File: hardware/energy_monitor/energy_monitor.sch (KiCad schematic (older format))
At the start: 46 parts, among them J1 Screw_Terminal_01x03, U1 RAC04, U2 ADS131E08

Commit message: Working on schematic
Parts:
- added C10, C11, C12, C17, C18, C19, C20, C21, C22, C23, C24, C26, C27, C28, C29, C3, C4, C5, C6, C7, C8: C, symbol C
- added D1, D10, D11, D12, D13, D14, D15, D16, D2, D3, D4, D5, D6, D7, D8, D9: BAV99, symbol D_Schottky_x2_Serial_AKC
- added D? (x6): D_TVS, symbol D_TVS
- added J2, J3, J4, J5, J6, J7: Audio-Jack-3, symbol Audio-Jack-3
- added R10, R13, R14, R15, R16, R17, R18, R19, R20, R21, R22, R23, R24, R25, R26, R27, R28, R29, R30, R9: R, symbol R
- gave numbers to parts that had none: 35
- renumbered C1 to C13, C2 to C14, C3 to C15, C4 to C16, U2 to U4
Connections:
- net labels added: I1_N, I1_P, I2_N, I2_P, I3_N, I3_P, I4_N, I4_P, I5_N, I5_P, I6_N, I6_P, L2_N, L2_P
- wire segments 139 -> 341
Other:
- moved on the sheet: C1, C13, C14, C15, C16, C2, C25, C30, C31, C32, C33, C34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

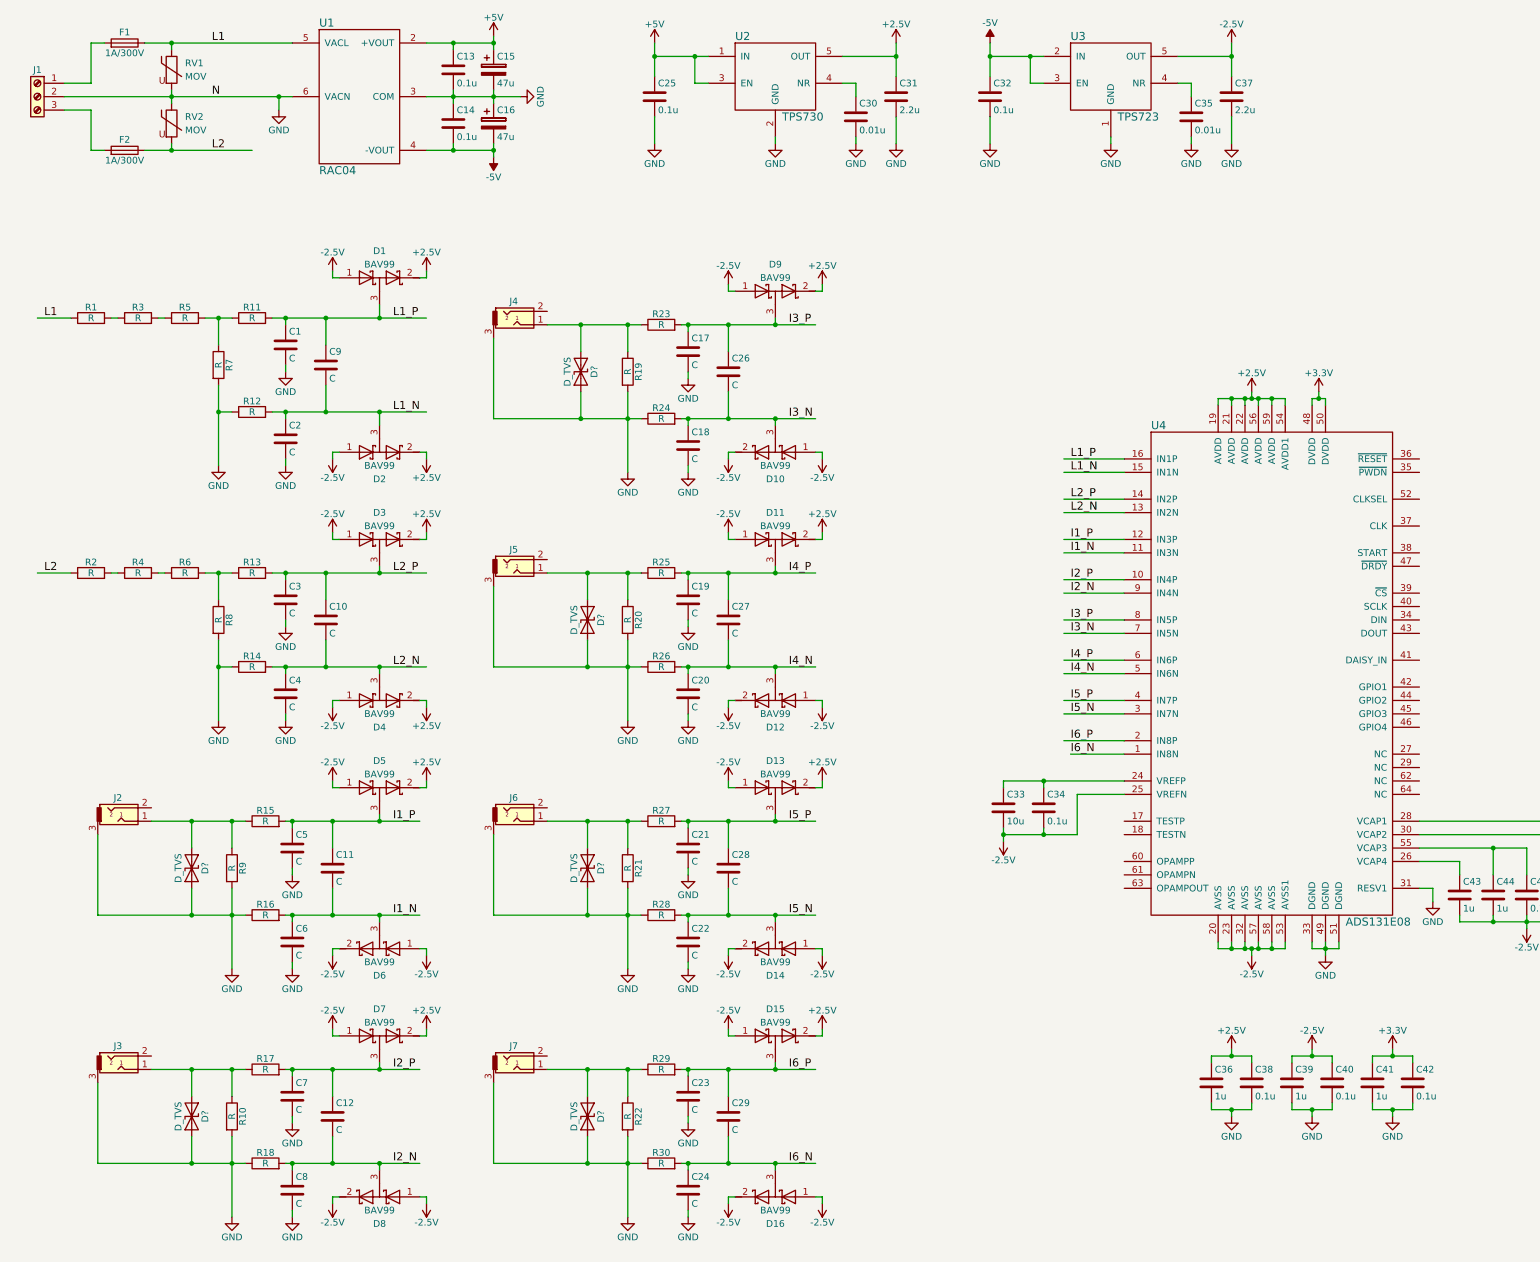
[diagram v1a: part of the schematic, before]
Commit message: Added footprints and part numbers for signal conditioning circuits
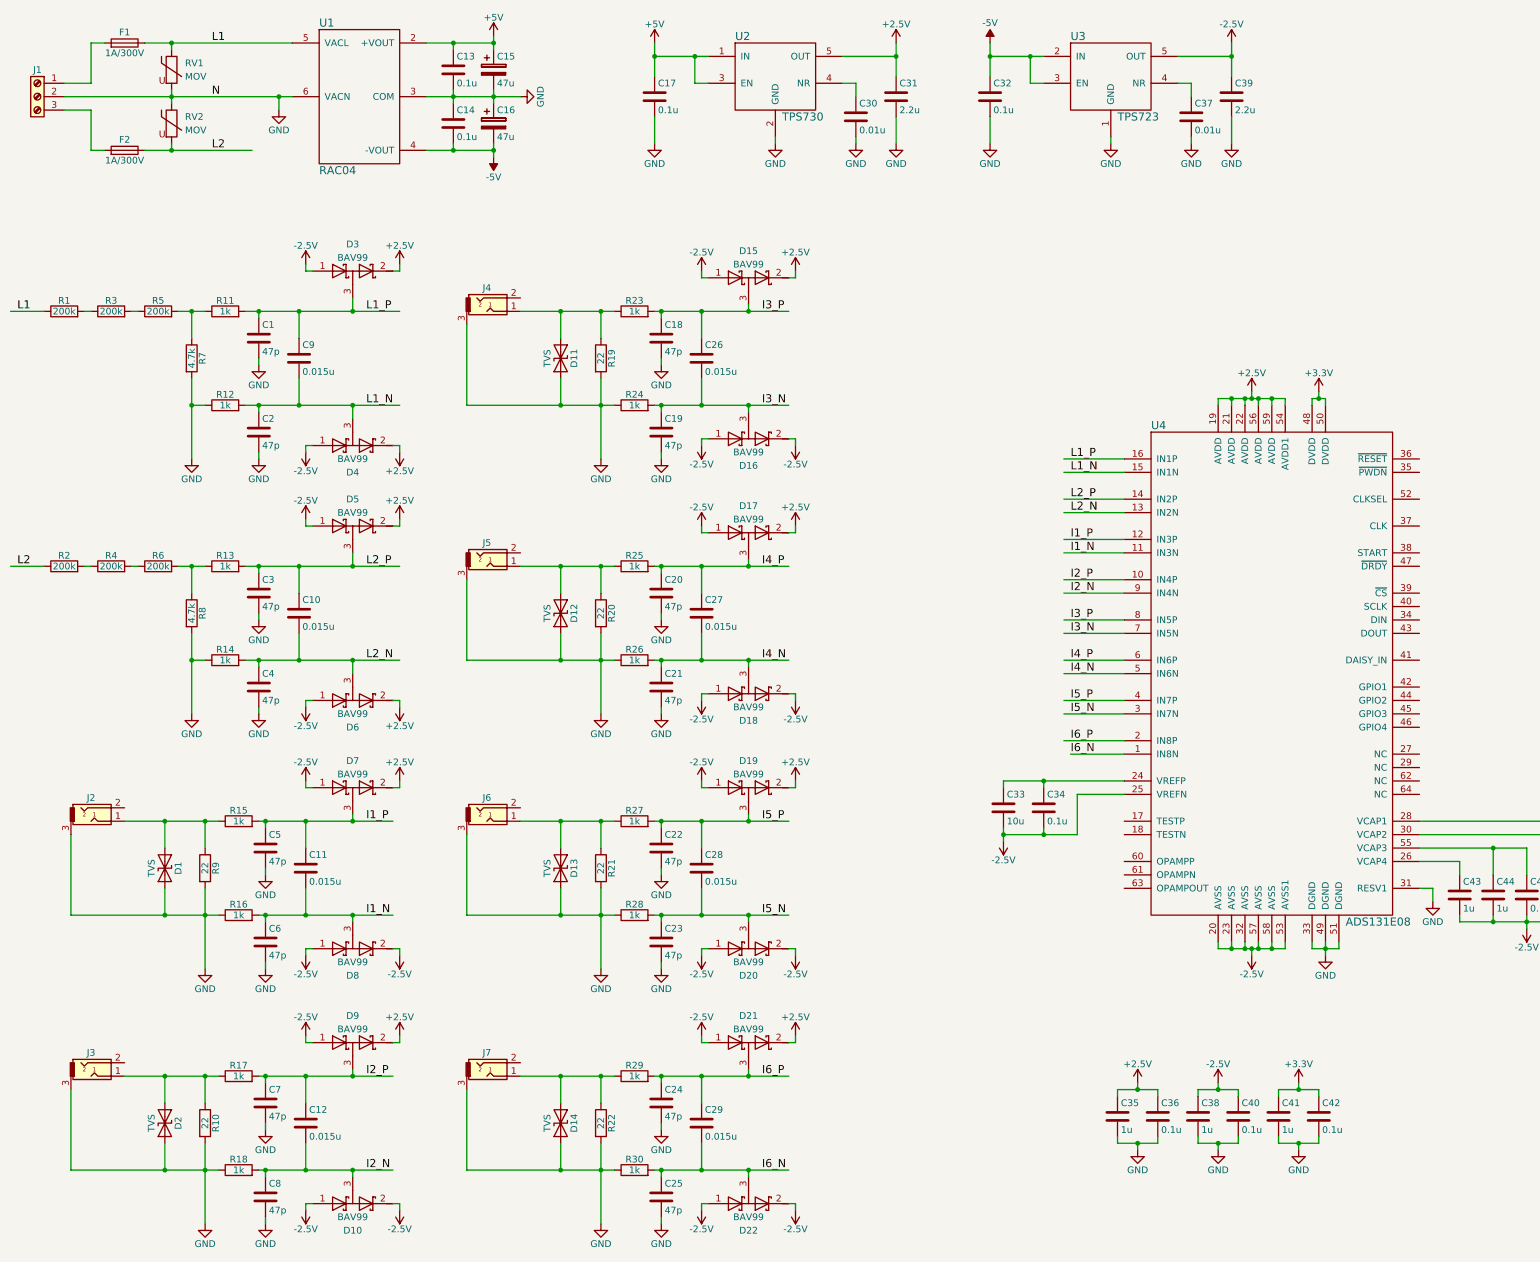
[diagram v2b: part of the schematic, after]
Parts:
- removed C17: C, symbol C
- removed D11, D12, D13, D14, D3, D4: BAV99, symbol D_Schottky_x2_Serial_AKC
- removed D? (x5): D_TVS, symbol D_TVS
- added C25: 47p, Capacitors_SMD:C_0603, symbol C
- added D11, D12, D13, D14, D2: TVS, Diodes_SMD:D_SMA, symbol D_TVS
- added D17, D18, D19, D20, D21, D22: BAV99, TO_SOT_Packages_SMD:SOT-23, symbol D_Schottky_x2_Serial_AKC
- C1, C18, C19, C2, C20, C21, C22, C23, C24, C3, C4, C5, C6, C7, C8: value C -> 47p; footprint (none) -> Capacitors_SMD:C_0603; Part (none) -> 490-4944-1-ND; Source (none) -> DigiKey
- C10, C11, C12, C26, C27, C28, C29, C9: value C -> 0.015u; footprint (none) -> Capacitors_SMD:C_0603; Part (none) -> 490-6054-1-ND; Source (none) -> DigiKey
- D1: renamed from D?; value D_TVS -> TVS; footprint (none) -> Diodes_SMD:D_SMA; Part (none) -> SMAJ5.0CA-FDICT-ND; Source (none) -> DigiKey
- D10, D15, D16, D5, D6, D7, D8, D9: footprint (none) -> TO_SOT_Packages_SMD:SOT-23; Part (none) -> BAV99-FDICT-ND; Source (none) -> DigiKey
- D3: renamed from D1; footprint (none) -> TO_SOT_Packages_SMD:SOT-23; Part (none) -> BAV99-FDICT-ND; Source (none) -> DigiKey
- D4: renamed from D2; footprint (none) -> TO_SOT_Packages_SMD:SOT-23; Part (none) -> BAV99-FDICT-ND; Source (none) -> DigiKey
- J2, J3, J4, J5, J6, J7: Part (none) -> CP-3524SJCT-ND; Source (none) -> DigiKey
- R1, R2, R3, R4, R5, R6: value R -> 200k; footprint (none) -> Resistors_SMD:R_1206; Part (none) -> 311-200KFRCT-ND; Source (none) -> DigiKey
- R10, R19, R20, R21, R22, R9: value R -> 22; footprint (none) -> Resistors_SMD:R_1206; Part (none) -> YAG3847CT-ND; Source (none) -> DigiKey
- R11, R12, R13, R14, R15, R16, R17, R18, R23, R24, R25, R26, R27, R28, R29, R30: value R -> 1k; footprint (none) -> Resistors_SMD:R_0603; Part (none) -> 311-1.00KHRCT-ND; Source (none) -> DigiKey
- R7, R8: value R -> 4.7k; footprint (none) -> Resistors_SMD:R_1206; Part (none) -> YAG2054CT-ND; Source (none) -> DigiKey
- renumbered C25 to C17, C36 to C35, C38 to C36, C35 to C37, C39 to C38, C37 to C39
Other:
- moved on the sheet: C1, C2, C35, C36, C38, C40, C41, C42, C9, D1, D3, D4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

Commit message: Working on schematic
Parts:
- added C?: 0.1u, symbol C
- added C?: 2.2u, symbol C
- added U?: AZ1117, TO_SOT_Packages_SMD:SOT-223-3_TabPin2, symbol AZ1117-3.3
- J1: Part (none) -> 277-1118-ND; Source (none) -> DigiKey
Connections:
- net labels added: CS, DRDY, MISO, MOSI, PWDN, RESET, SCLK, START
- wire segments 341 -> 360
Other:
- moved on the sheet: C17, C30, C31, C32, C33, C34, C37, C39, C43, C44, C45, C46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

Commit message: Working on schematic
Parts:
- removed U?: AZ1117, TO_SOT_Packages_SMD:SOT-223-3_TabPin2, symbol AZ1117-3.3
- added C50: 0.1u, symbol C
- added C51: 10u, symbol C
- added C52: 4.7u, symbol C
- added D23, D27: RED, Diodes_SMD:D_0603, symbol LED
- added D24, D28: GRN, Diodes_SMD:D_0603, symbol LED
- added D25, D26: MBR120, symbol D_Schottky
- added J8: USB_OTG, symbol USB_OTG
- added Q1, Q2: MMBT2222, symbol Q_NPN_BEC
- added R31, R32, R36, R37: 1k, Resistors_SMD:R_0603, symbol R
- added R33, R34, R35: 10k, symbol R
- added U5: AP2112, symbol AP2112
- added U7: CP2104, symbol CP2104
- C49: renamed from C?; value 2.2u -> 10u
- gave numbers to parts that had none: 1
- renumbered C37 to C36, C36 to C37, C39 to C38, C38 to C39, C43 to C44, C44 to C45, C45 to C46, C46 to C47, C47 to C48, U5 to U6
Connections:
- net labels added: DTR, D_N, D_P, GPIO0, LED, RTS, RXD0, SCK, TXD0, VUSB
- net labels removed: SCLK
- wire segments 360 -> 430
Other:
- moved on the sheet: C1, C10, C11, C12, C13, C14, C15, C16, C17, C18, C19, C2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
